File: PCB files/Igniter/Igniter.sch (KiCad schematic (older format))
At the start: 26 parts, among them J1 PT2, J2 PT1, J3 PT4, J4 PT3, J5 Conn_01x02_Female, J6 IgnitionCoil, J7 SD Header, Q1 N MOSFET, SW1 Keylock, SW3 Ignite

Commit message: 10/27/2019
More 2560 pins named/connected
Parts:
- XA1: symbol arduino:Arduino_Mega2560_Shield -> Igniter-rescue:Arduino_Mega2560_Shield-arduino
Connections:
- net labels added: CLK, CS, DI, DO
- wire segments 41 -> 47
- no-connect marks 1 -> 6
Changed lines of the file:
@@
 LIBS:interface
 LIBS:Igniter-cache
-EELAYER 26 0
+EELAYER 29 0
 EELAYER END
 $Descr A 11000 8500
@@
 Connection ~ 8930 4720
 $Comp
-L arduino:Arduino_Mega2560_Shield XA1
+L Igniter-rescue:Arduino_Mega2560_Shield-arduino XA1
 U 1 1 5DB49E1D
 P 5045 4260
@@
 Wire Wire Line
 	8930 5070 8930 5515
-Text Notes 9105 4840 0    50   ~ 0
+Text Notes 9095 4930 0    157  ~ 31
 *
 $Comp
@@
 U 1 1 5DB4BEEA
 P 2015 1740
-F 0 "MH4" H 1915 1740 50  0000 R CNN
+F 0 "MH4" H 1915 1740 50  0001 R CNN
 F 1 "MountingHole" H 2115 1695 50  0001 L CNN
 F 2 "MountingHole:MountingHole_2.2mm_M2" H 2015 1740 50  0001 C CNN
@@
 	1    0    0    -1
 $EndComp
+$Comp
+L power:+5V #PWR?
+U 1 1 5DB69B91
+P 1805 1730
+F 0 "#PWR?" H 1805 1580 50  0001 C CNN
+F 1 "+5V" H 1820 1903 50  0000 C CNN
+F 2 "" H 1805 1730 50  0001 C CNN
+F 3 "" H 1805 1730 50  0001 C CNN
+	1    1805 1730
+	1    0    0    -1
+$EndComp
+NoConn ~ 1505 1630
+$Comp
+L power:GNDREF #PWR?
+U 1 1 5DB6CE1B
+P 1660 1530
+F 0 "#PWR?" H 1660 1280 50  0001 C CNN
+F 1 "GNDREF" H 1665 1357 50  0001 C CNN
+F 2 "" H 1660 1530 50  0001 C CNN
+F 3 "" H 1660 1530 50  0001 C CNN
+	1    1660 1530
+	1    0    0    -1
+$EndComp
+Wire Wire Line
+	1660 1530 1505 1530
+Wire Wire Line
+	1505 1730 1805 1730
+NoConn ~ 1505 1030
+Text GLabel 4995 1660 1    50   Input ~ 0
+CLK
+Text GLabel 1505 1430 2    50   Input ~ 0
+CLK
+Text GLabel 1505 1330 2    50   Input ~ 0
+DO
+Text GLabel 1505 1230 2    50   Input ~ 0
+DI
+Text GLabel 1505 1130 2    50   Input ~ 0
+CS
+Text GLabel 6345 6410 2    50   Input ~ 0
+CS
+Text GLabel 4895 1660 1    50   Input ~ 0
+DI
+Text GLabel 4795 1660 1    50   Input ~ 0
+DO
+$Comp
+L power:GNDREF #PWR?
+U 1 1 5DB796A8
+P 5265 1485
+F 0 "#PWR?" H 5265 1235 50  0001 C CNN
+F 1 "GNDREF" H 5270 1312 50  0001 C CNN
+F 2 "" H 5265 1485 50  0001 C CNN
+F 3 "" H 5265 1485 50  0001 C CNN
+	1    5265 1485
+	1    0    0    -1
+$EndComp
+Wire Wire Line
+	5195 1660 5195 1485
+Wire Wire Line
+	5195 1485 5265 1485
+NoConn ~ 3745 5010
+Wire Wire Line
+	3745 6310 3745 6210
+Wire Wire Line
+	3745 6110 3745 6210
+Connection ~ 3745 6110
+Connection ~ 3745 6210
+NoConn ~ 3745 6010
+NoConn ~ 6345 2710
 $EndSCHEMATC

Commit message: 10/28/2019
Added footprint for resettable fuse
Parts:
- F1: footprint (none) -> Resistor_THT:R_Axial_DIN0204_L3.6mm_D1.6mm_P5.08mm_Horizontal
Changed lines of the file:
@@
 LIBS:interface
 LIBS:Igniter-cache
-EELAYER 29 0
+EELAYER 26 0
 EELAYER END
 $Descr A 11000 8500
@@
 F 0 "F1" H 9215 1231 50  0000 L CNN
 F 1 "Fuse" H 9215 1140 50  0000 L CNN
-F 2 "" V 9085 1185 50  0001 C CNN
+F 2 "Resistor_THT:R_Axial_DIN0204_L3.6mm_D1.6mm_P5.08mm_Horizontal" V 9085 1185 50  0001 C CNN
 F 3 "~" H 9155 1185 50  0001 C CNN
 	1    9155 1185
@@
 Size this guy
 $Comp
-L power:+5V #PWR?
+L power:+5V #PWR0101
 U 1 1 5DB63DDE
 P 2975 2110
-F 0 "#PWR?" H 2975 1960 50  0001 C CNN
+F 0 "#PWR0101" H 2975 1960 50  0001 C CNN
 F 1 "+5V" H 2990 2283 50  0000 C CNN
 F 2 "" H 2975 2110 50  0001 C CNN
@@
 $EndComp
 $Comp
-L power:+5V #PWR?
+L power:+5V #PWR0102
 U 1 1 5DB69B91
 P 1805 1730
-F 0 "#PWR?" H 1805 1580 50  0001 C CNN
+F 0 "#PWR0102" H 1805 1580 50  0001 C CNN
 F 1 "+5V" H 1820 1903 50  0000 C CNN
 F 2 "" H 1805 1730 50  0001 C CNN
@@
 NoConn ~ 1505 1630
 $Comp
-L power:GNDREF #PWR?
+L power:GNDREF #PWR0105
 U 1 1 5DB6CE1B
 P 1660 1530
-F 0 "#PWR?" H 1660 1280 50  0001 C CNN
+F 0 "#PWR0105" H 1660 1280 50  0001 C CNN
 F 1 "GNDREF" H 1665 1357 50  0001 C CNN
 F 2 "" H 1660 1530 50  0001 C CNN
@@
 DO
 $Comp
-L power:GNDREF #PWR?
+L power:GNDREF #PWR0117
 U 1 1 5DB796A8
 P 5265 1485
-F 0 "#PWR?" H 5265 1235 50  0001 C CNN
+F 0 "#PWR0117" H 5265 1235 50  0001 C CNN
 F 1 "GNDREF" H 5270 1312 50  0001 C CNN
 F 2 "" H 5265 1485 50  0001 C CNN

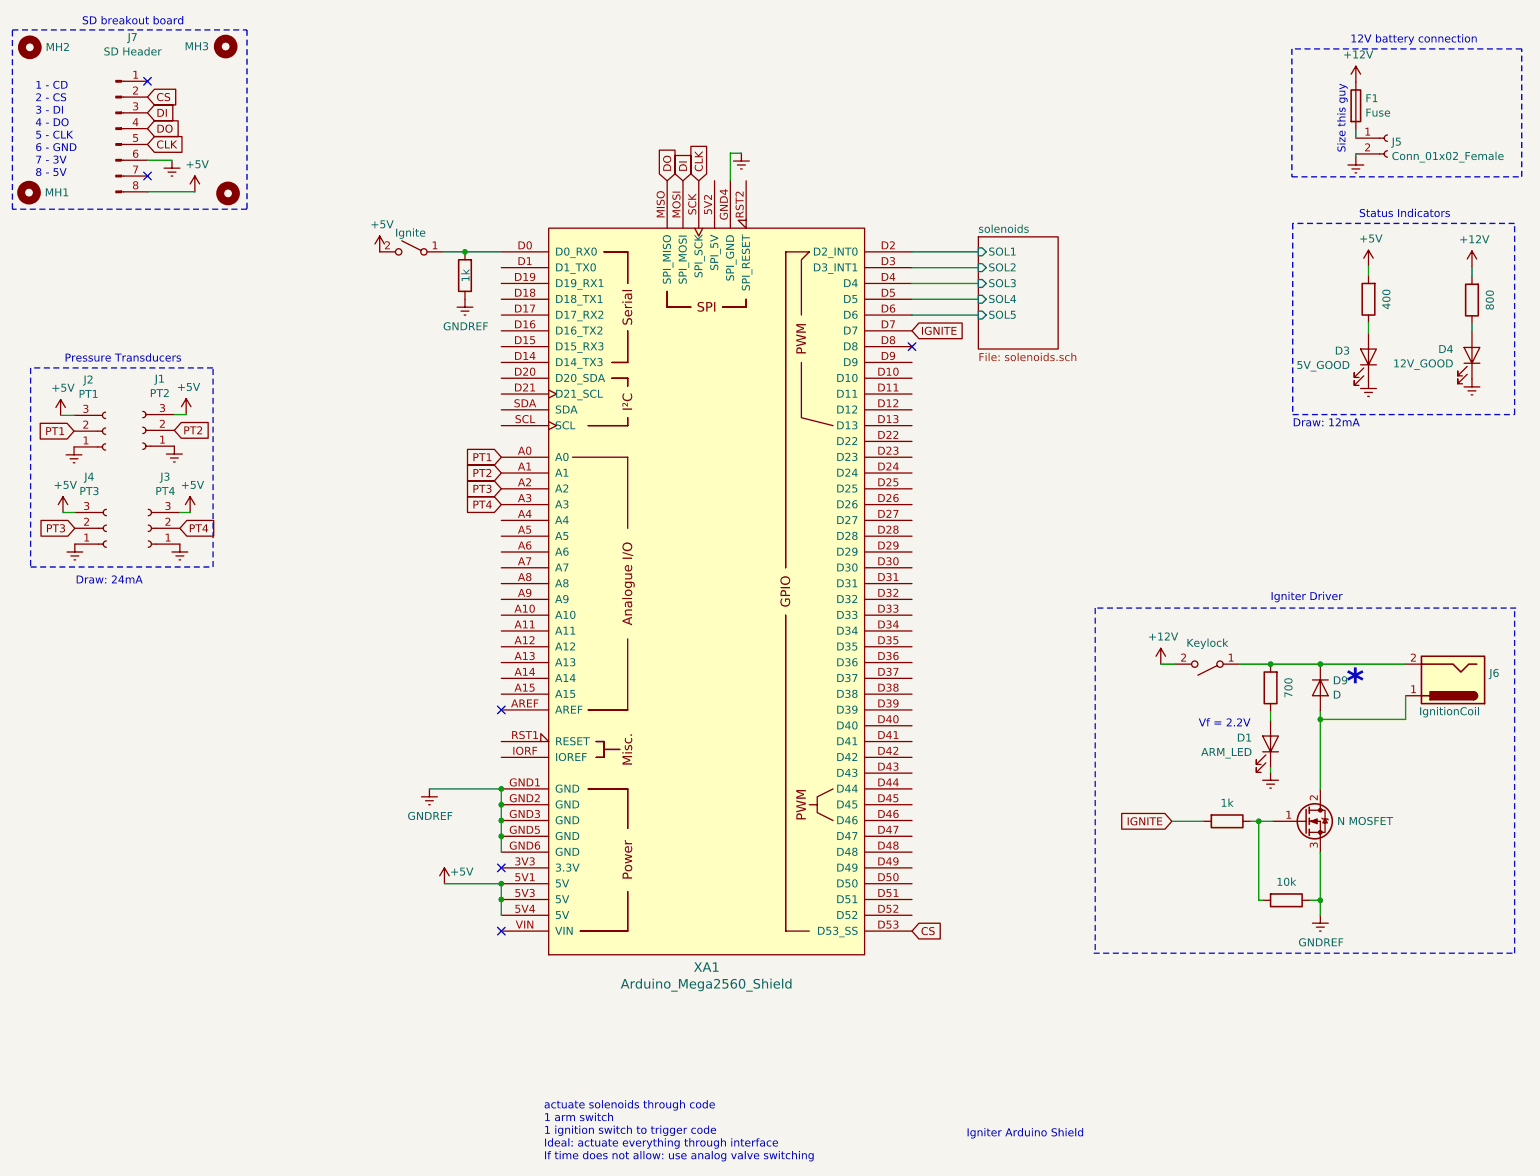
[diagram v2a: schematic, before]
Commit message: 10/30/2019
-Changed igniter switch circuit to include indicator
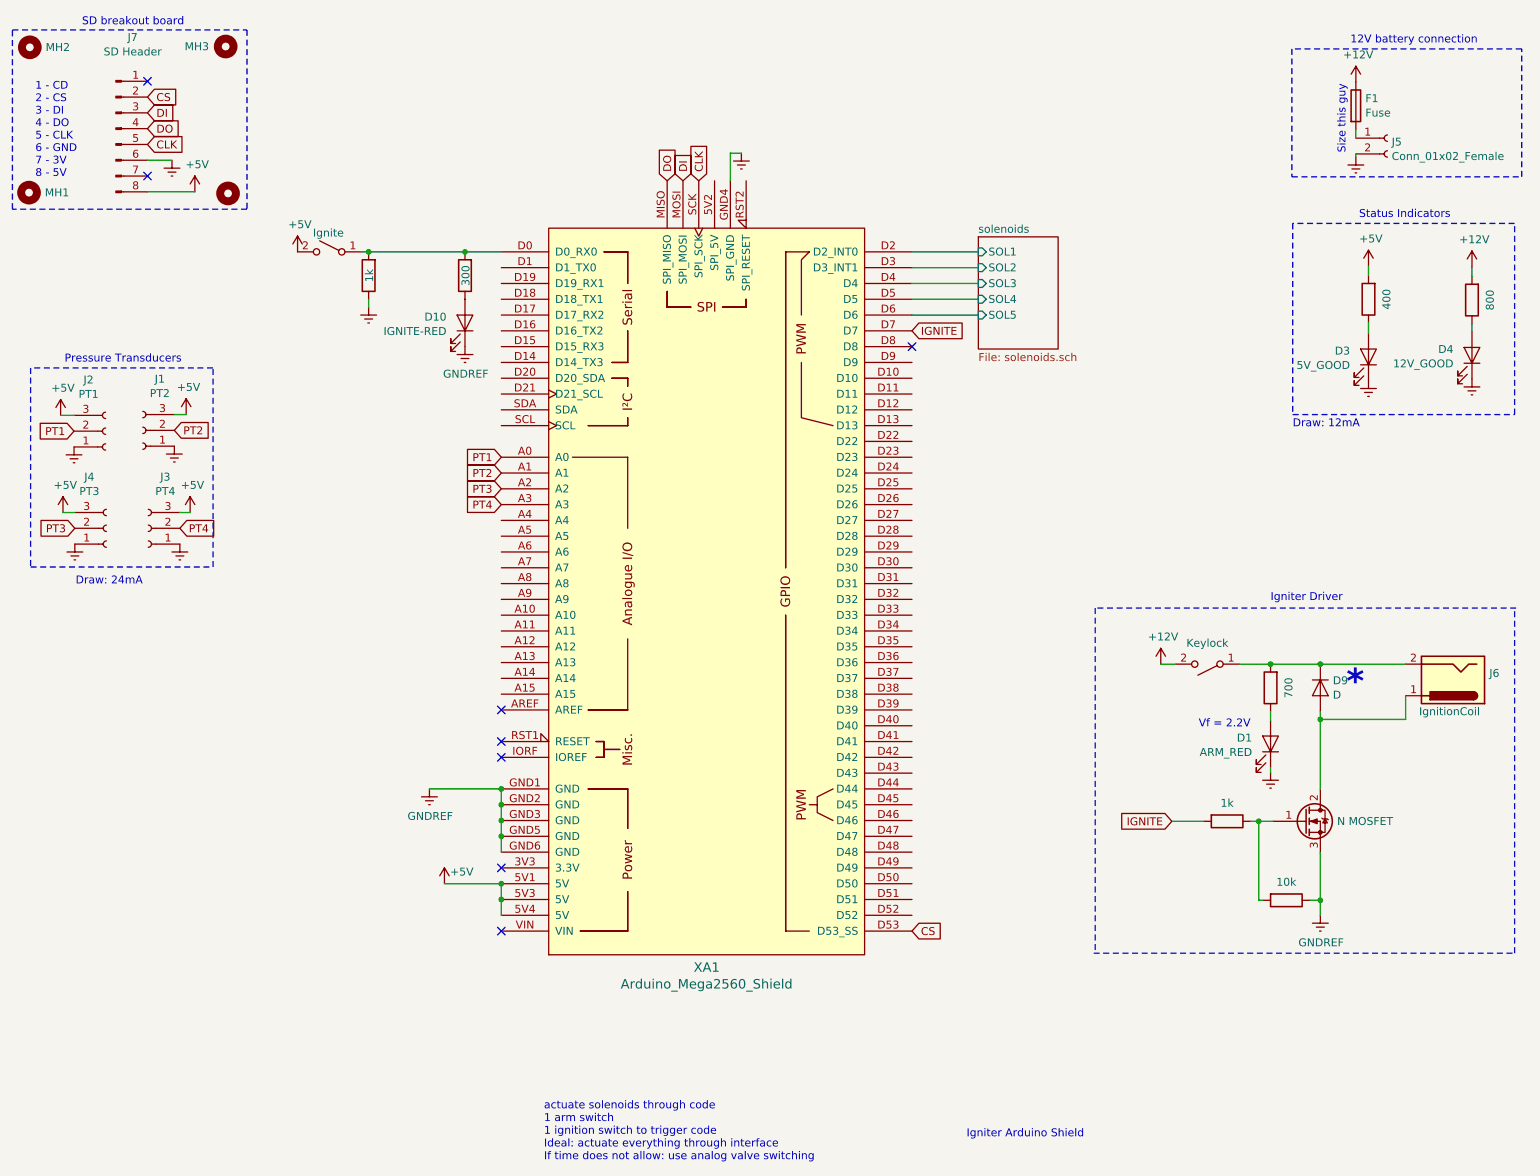
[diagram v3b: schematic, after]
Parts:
- added D10: IGNITE-RED, LED_THT:LED_D3.0mm, symbol Device:LED
- added R?: 1k, Resistor_THT:R_Axial_DIN0204_L3.6mm_D1.6mm_P5.08mm_Horizontal, symbol Device:R
- D1: value ARM_LED -> ARM_RED
- R4: value 1k -> 300
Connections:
- net GNDREF: now also D10.1 (K), R?.1; no longer R4.1
- net at R4.2, SW3.1 (A), XA1.D0 (D0_RX0): now also R?.2
- new net: D10.2 (A), R4.1
- no-connect marks 6 -> 8
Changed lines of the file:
@@
 LIBS:interface
 LIBS:Igniter-cache
-EELAYER 26 0
+EELAYER 29 0
 EELAYER END
 $Descr A 11000 8500
@@
 AR Path="/5DAB74FF" Ref="D1"  Part="1"
 F 0 "D1" V 8653 5108 50  0000 R CNN
-F 1 "ARM_LED" V 8562 5108 50  0000 R CNN
+F 1 "ARM_RED" V 8562 5108 50  0000 R CNN
 F 2 "LED_THT:LED_D3.0mm" H 8615 5225 50  0001 C CNN
 F 3 "~" H 8615 5225 50  0001 C CNN
@@
 L Switch:SW_SPST SW?
 U 1 1 5DB5112B
-P 3175 2110
+P 2655 2110
 AR Path="/5D9BEB88/5DB5112B" Ref="SW?"  Part="1"
 AR Path="/5DB5112B" Ref="SW3"  Part="1"
-F 0 "SW3" H 3175 1885 50  0001 C CNN
-F 1 "Ignite" H 3180 2230 50  0000 C CNN
-F 2 "" H 3175 2110 50  0001 C CNN
-F 3 "~" H 3175 2110 50  0001 C CNN
-	1    3175 2110
+F 0 "SW3" H 2655 1885 50  0001 C CNN
+F 1 "Ignite" H 2660 2230 50  0000 C CNN
+F 2 "" H 2655 2110 50  0001 C CNN
+F 3 "~" H 2655 2110 50  0001 C CNN
+	1    2655 2110
 	-1   0    0    -1
 $EndComp
-Wire Wire Line
-	3375 2110 3515 2110
 $Comp
 L power:GNDREF #PWR0103
 U 1 1 5DB519E7
-P 3515 2410
-F 0 "#PWR0103" H 3515 2160 50  0001 C CNN
-F 1 "GNDREF" H 3520 2237 50  0000 C CNN
-F 2 "" H 3515 2410 50  0001 C CNN
-F 3 "" H 3515 2410 50  0001 C CNN
-	1    3515 2410
+P 3515 2710
+F 0 "#PWR0103" H 3515 2460 50  0001 C CNN
+F 1 "GNDREF" H 3520 2537 50  0000 C CNN
+F 2 "" H 3515 2710 50  0001 C CNN
+F 3 "" H 3515 2710 50  0001 C CNN
+	1    3515 2710
 	1    0    0    -1
 $EndComp
@@
 AR Path="/5DB51A4D" Ref="R4"  Part="1"
 F 0 "R4" V 3308 2260 50  0001 C CNN
-F 1 "1k" V 3510 2260 50  0000 C CNN
+F 1 "300" V 3510 2260 50  0000 C CNN
 F 2 "Resistor_THT:R_Axial_DIN0204_L3.6mm_D1.6mm_P5.08mm_Horizontal" V 3445 2260 50  0001 C CNN
 F 3 "~" H 3515 2260 50  0001 C CNN
@@
 L power:+5V #PWR0101
 U 1 1 5DB63DDE
-P 2975 2110
-F 0 "#PWR0101" H 2975 1960 50  0001 C CNN
-F 1 "+5V" H 2990 2283 50  0000 C CNN
-F 2 "" H 2975 2110 50  0001 C CNN
-F 3 "" H 2975 2110 50  0001 C CNN
-	1    2975 2110
+P 2455 2110
+F 0 "#PWR0101" H 2455 1960 50  0001 C CNN
+F 1 "+5V" H 2470 2283 50  0000 C CNN
+F 2 "" H 2455 2110 50  0001 C CNN
+F 3 "" H 2455 2110 50  0001 C CNN
+	1    2455 2110
 	1    0    0    -1
 $EndComp
@@
 NoConn ~ 3745 6010
 NoConn ~ 6345 2710
+$Comp
+L Device:LED D?
+U 1 1 5DB95140
+P 3515 2560
+AR Path="/5D9BEB88/5DB95140" Ref="D?"  Part="1"
+AR Path="/5DB95140" Ref="D10"  Part="1"
+F 0 "D10" V 3553 2443 50  0000 R CNN
+F 1 "IGNITE-RED" V 3462 2443 50  0000 R CNN
+F 2 "LED_THT:LED_D3.0mm" H 3515 2560 50  0001 C CNN
+F 3 "~" H 3515 2560 50  0001 C CNN
+	1    3515 2560
+	0    1    -1   0
+$EndComp
+NoConn ~ 3745 5310
+NoConn ~ 3745 5210
+$Comp
+L Device:R R?
+U 1 1 5DBA787B
+P 2905 2260
+AR Path="/5D9BEB88/5DBA787B" Ref="R?"  Part="1"
+AR Path="/5DBA787B" Ref="R?"  Part="1"
+F 0 "R?" V 2698 2260 50  0001 C CNN
+F 1 "1k" V 2900 2260 50  0000 C CNN
+F 2 "Resistor_THT:R_Axial_DIN0204_L3.6mm_D1.6mm_P5.08mm_Horizontal" V 2835 2260 50  0001 C CNN
+F 3 "~" H 2905 2260 50  0001 C CNN
+	1    2905 2260
+	-1   0    0    1
+$EndComp
+$Comp
+L power:GNDREF #PWR?
+U 1 1 5DBA8069
+P 2905 2460
+F 0 "#PWR?" H 2905 2210 50  0001 C CNN
+F 1 "GNDREF" H 2910 2287 50  0001 C CNN
+F 2 "" H 2905 2460 50  0001 C CNN
+F 3 "" H 2905 2460 50  0001 C CNN
+	1    2905 2460
+	1    0    0    -1
+$EndComp
+Wire Wire Line
+	2855 2110 2905 2110
+Connection ~ 2905 2110
+Wire Wire Line
+	2905 2110 3515 2110
+Wire Wire Line
+	2905 2410 2905 2460
 $EndSCHEMATC

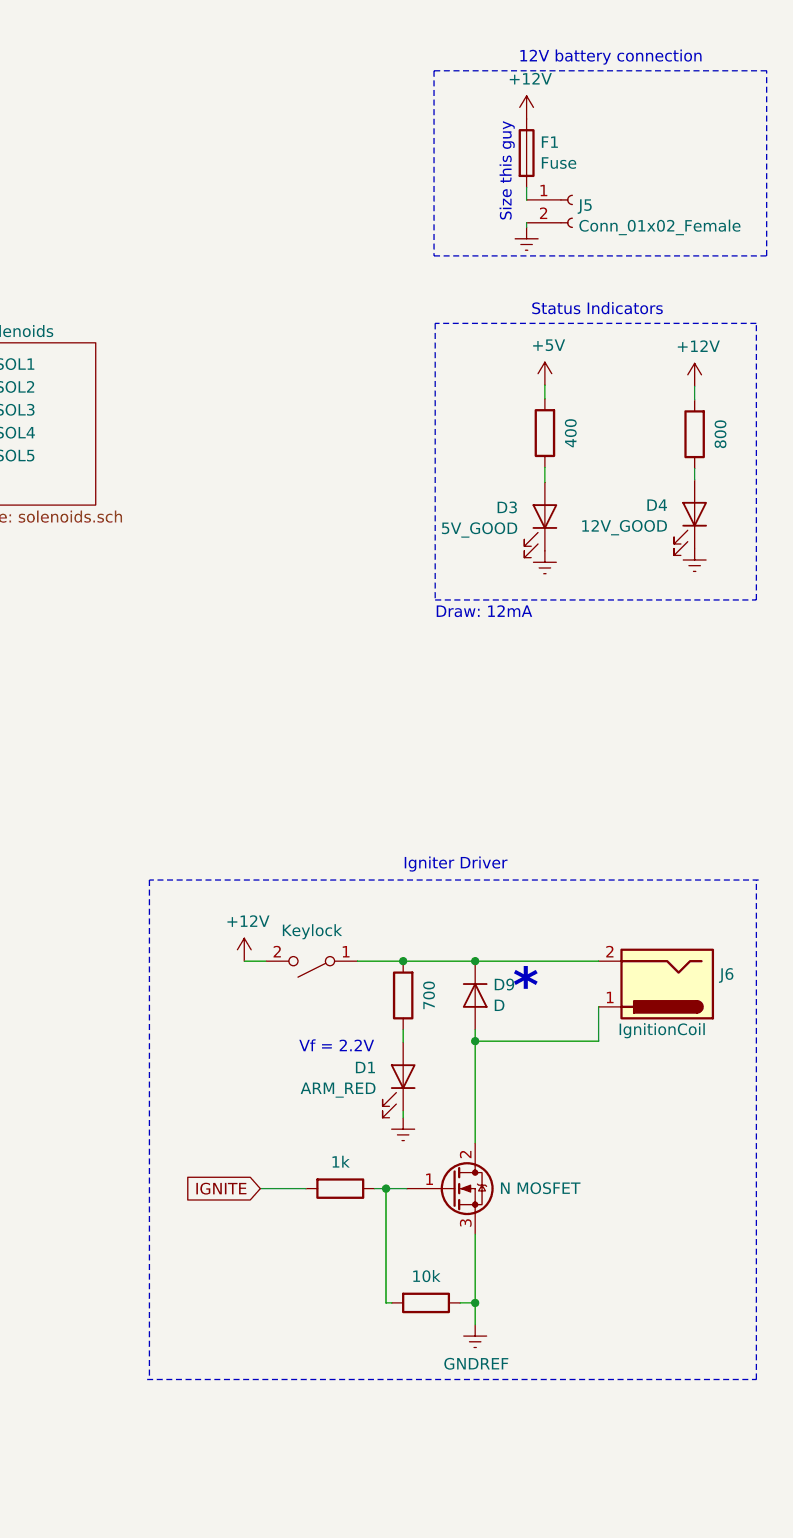
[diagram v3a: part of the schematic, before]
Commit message: 10/30/2019
-Moved keylock
-Removed 1k from MOSFET gates, wasnt adding anything useful to the circuit
-Updated battery voltage to 24V
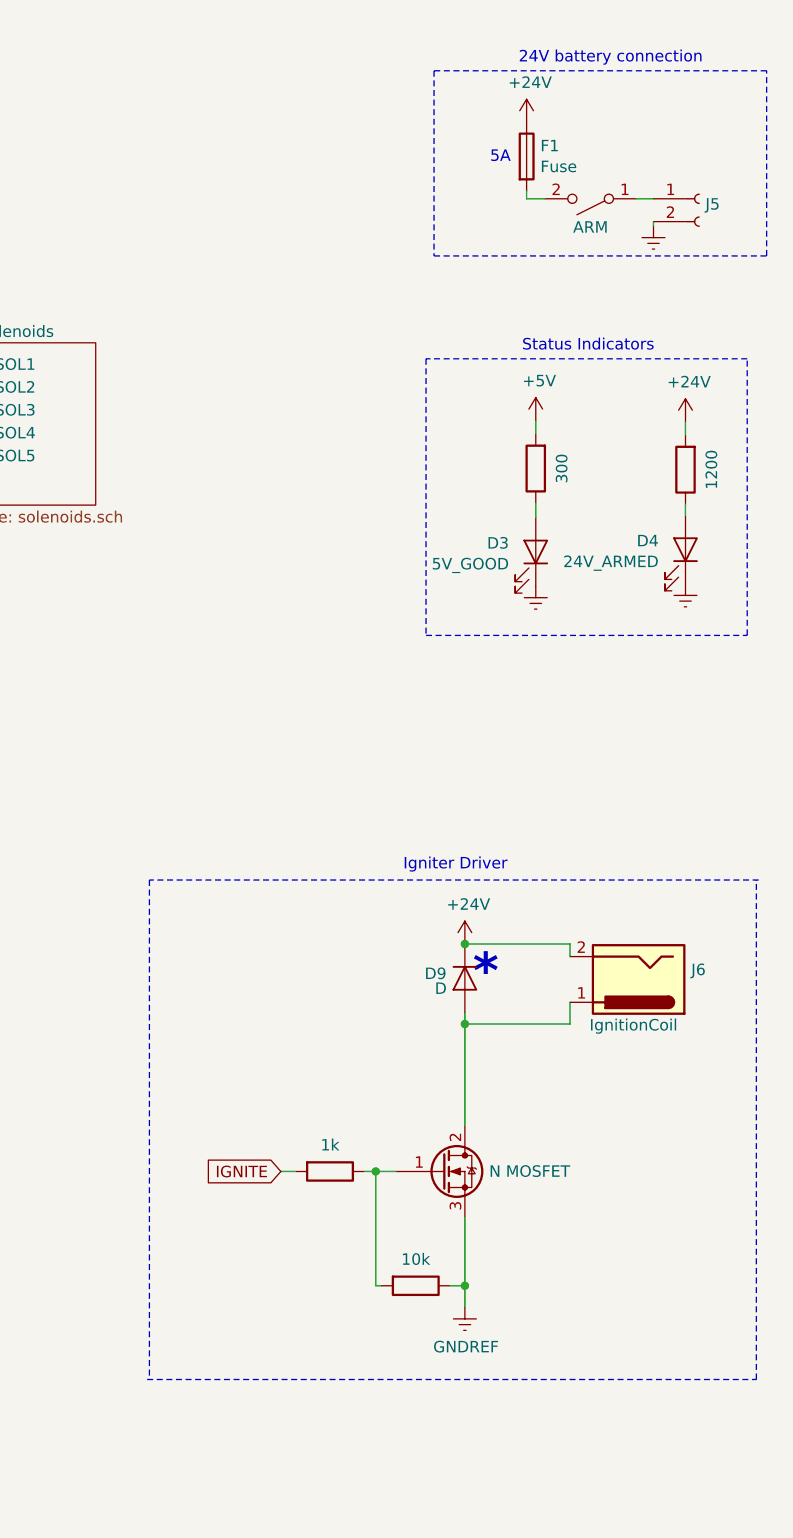
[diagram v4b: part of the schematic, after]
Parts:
- removed D1: ARM_RED, LED_THT:LED_D3.0mm, symbol Device:LED
- removed R2: 700, Resistor_THT:R_Axial_DIN0204_L3.6mm_D1.6mm_P5.08mm_Horizontal, symbol Device:R
- D4: value 12V_GOOD -> 24V_ARMED
- R5: value 400 -> 300
- R6: value 800 -> 1200
- SW1: value Keylock -> ARM
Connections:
- net +24V: now reaches D9.1 (K), J6.2
- net +24V: now also F1.1, R6.2; no longer SW1.1 (A)
- net at J5.1 (Pin_1): now also SW1.1 (A); no longer F1.2
- removed net +12V: F1.1, R6.2, SW1.2 (B)
- new net: F1.2, SW1.2 (B)
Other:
- note added: "24V battery connection"
- note added: "5A"
- note removed: "12V battery connection"
- note removed: "Draw: 12mA"
- note removed: "Size this guy"
- note removed: "Vf = 2.2V\n"
- moved on the sheet: D3, D4, D9, J5, J6
